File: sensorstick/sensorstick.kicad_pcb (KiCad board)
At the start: 2 copper layers, 85 x 23 mm, 10 parts, among them J1 U217-04XN-XXR84, U1 XIAO-ESP32-C6-SMD, U2 SCD40-D-R2

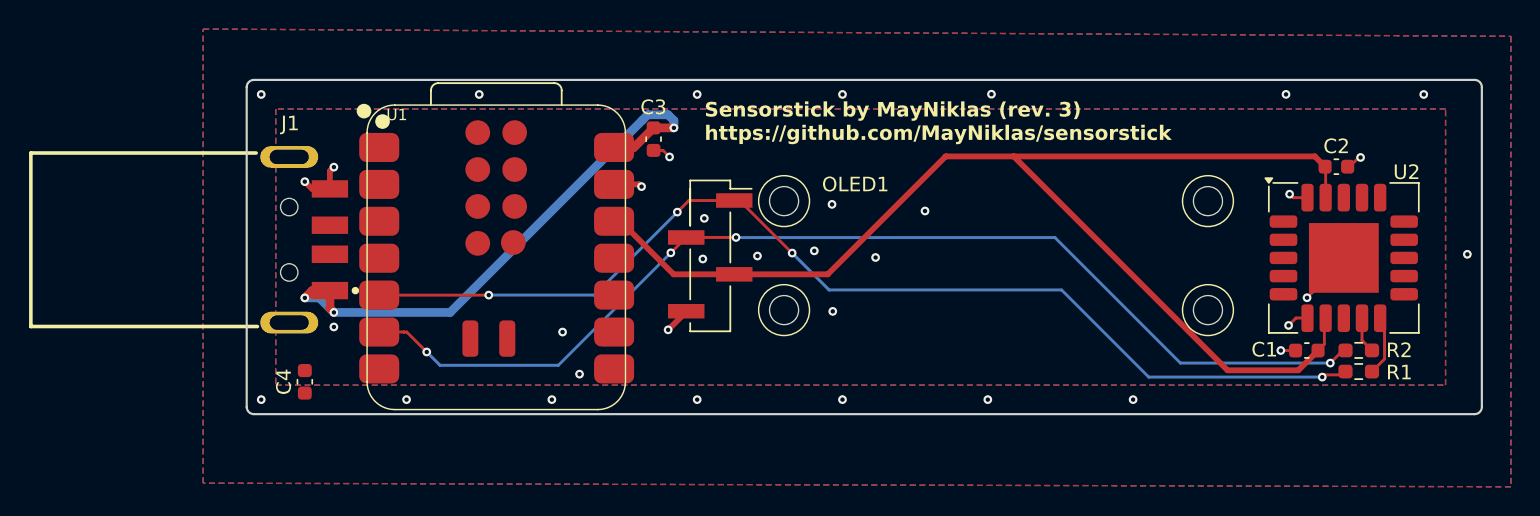
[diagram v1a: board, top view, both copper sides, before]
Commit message: remove unused pads
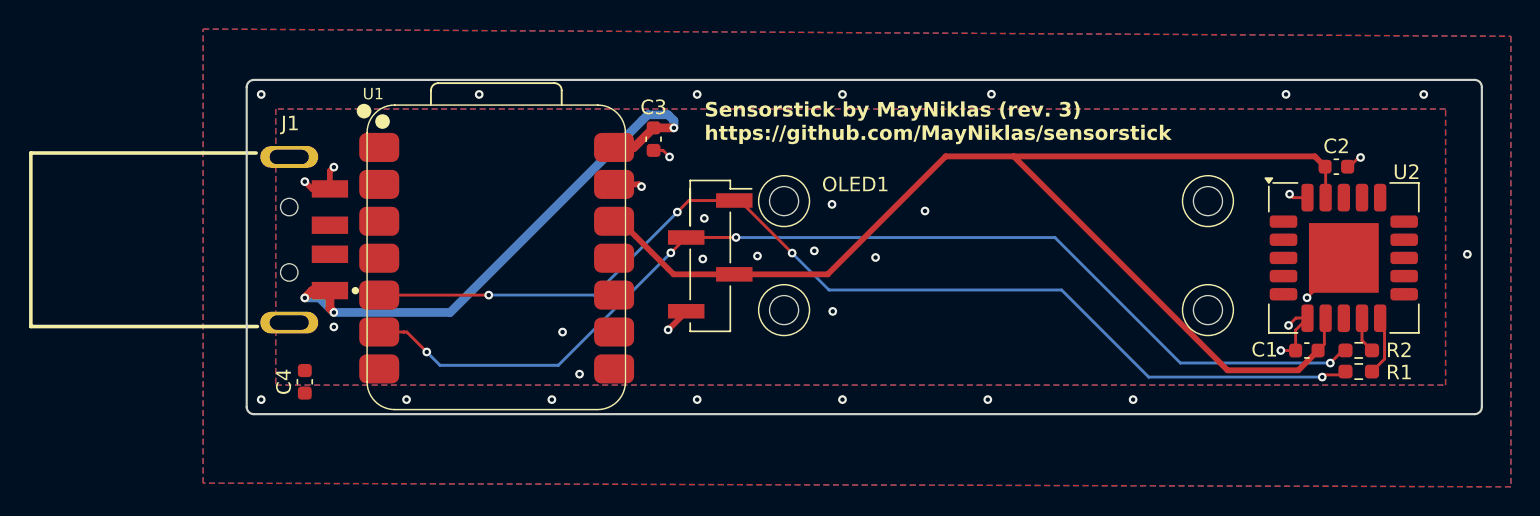
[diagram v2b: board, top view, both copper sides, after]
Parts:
- U1: footprint CustomLibrary:XIAO-ESP32C6-SMD -> CustomLibrary:XIAO-ESP32C6-SMD_no-pad
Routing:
- net GND: track 17.7 -> 20.3 mm
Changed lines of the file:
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@@
 	(net 10 "Net-(U2-SCL)")
 	(net 11 "unconnected-(U1-GPIO18_D10_MOSI-Pad11)")
-	(net 12 "unconnected-(U1-CHIP_EN-Pad19)")
-	(net 13 "unconnected-(U1-GPIO20_D9_MISO-Pad10)")
-	(net 14 "unconnected-(U1-3V3_1-Pad24)")
-	(net 15 "unconnected-(U1-MTDO-Pad18)")
-	(net 16 "unconnected-(U1-MTMS-Pad21)")
-	(net 17 "unconnected-(U1-GPIO19_D8_SCK-Pad9)")
-	(net 18 "unconnected-(U1-GPIO0_A0_D0-Pad1)")
-	(net 19 "unconnected-(U1-GPIO17_D7_RX-Pad8)")
-	(net 20 "unconnected-(U1-GPIO1_A1_D1-Pad2)")
-	(net 21 "unconnected-(U1-GPIO21_D3-Pad4)")
-	(net 22 "unconnected-(U1-GPIO2_A2_D2-Pad3)")
-	(net 23 "unconnected-(U1-MTCK-Pad22)")
-	(net 24 "unconnected-(U1-GPIO16_D6_TX-Pad7)")
-	(net 25 "unconnected-(U1-BOOT-Pad23)")
-	(net 26 "unconnected-(U1-MTDI-Pad17)")
-	(net 27 "unconnected-(U1-GND-Pad20)")
-	(net 28 "unconnected-(U1-GND-Pad16)")
-	(net 29 "unconnected-(U1-BAT-Pad15)")
+	(net 12 "unconnected-(U1-GPIO20_D9_MISO-Pad10)")
+	(net 13 "unconnected-(U1-GPIO19_D8_SCK-Pad9)")
+	(net 14 "unconnected-(U1-GPIO0_A0_D0-Pad1)")
+	(net 15 "unconnected-(U1-GPIO17_D7_RX-Pad8)")
+	(net 16 "unconnected-(U1-GPIO1_A1_D1-Pad2)")
+	(net 17 "unconnected-(U1-GPIO21_D3-Pad4)")
+	(net 18 "unconnected-(U1-GPIO2_A2_D2-Pad3)")
+	(net 19 "unconnected-(U1-GPIO16_D6_TX-Pad7)")
 	(footprint "Capacitor_SMD:C_0603_1608Metric"
 		(layer "F.Cu")
@@
 		)
 	)
-	(footprint "CustomLibrary:XIAO-ESP32C6-SMD"
+	(footprint "CustomLibrary:XIAO-ESP32C6-SMD_no-pad"
 		(layer "F.Cu")
 		(at 77.4 99.7468)
 		(property "Reference" "U1"
-			(at -7.7986 -9.3825 0)
+			(at -9.425 -10.8218 0)
 			(layer "F.SilkS")
 			(effects
@@
 			(layers "F.Cu" "F.Mask" "F.Paste")
 			(roundrect_rratio 0.25)
-			(net 18 "unconnected-(U1-GPIO0_A0_D0-Pad1)")
+			(net 14 "unconnected-(U1-GPIO0_A0_D0-Pad1)")
 			(pinfunction "GPIO0_A0_D0")
 			(pintype "passive+no_connect")
@@
 			(layers "F.Cu" "F.Mask" "F.Paste")
 			(roundrect_rratio 0.25)
-			(net 20 "unconnected-(U1-GPIO1_A1_D1-Pad2)")
+			(net 16 "unconnected-(U1-GPIO1_A1_D1-Pad2)")
 			(pinfunction "GPIO1_A1_D1")
 			(pintype "passive+no_connect")
@@
 			(layers "F.Cu" "F.Mask" "F.Paste")
 			(roundrect_rratio 0.25)
-			(net 22 "unconnected-(U1-GPIO2_A2_D2-Pad3)")
+			(net 18 "unconnected-(U1-GPIO2_A2_D2-Pad3)")
 			(pinfunction "GPIO2_A2_D2")
 			(pintype "passive+no_connect")
@@
 			(layers "F.Cu" "F.Mask" "F.Paste")
 			(roundrect_rratio 0.25)
-			(net 21 "unconnected-(U1-GPIO21_D3-Pad4)")
+			(net 17 "unconnected-(U1-GPIO21_D3-Pad4)")
 			(pinfunction "GPIO21_D3")
 			(pintype "passive+no_connect")
@@
 			(layers "F.Cu" "F.Mask" "F.Paste")
 			(roundrect_rratio 0.25)
-			(net 24 "unconnected-(U1-GPIO16_D6_TX-Pad7)")
+			(net 19 "unconnected-(U1-GPIO16_D6_TX-Pad7)")
 			(pinfunction "GPIO16_D6_TX")
 			(pintype "passive+no_connect")
@@
 			(layers "F.Cu" "F.Mask" "F.Paste")
 			(roundrect_rratio 0.25)
-			(net 19 "unconnected-(U1-GPIO17_D7_RX-Pad8)")
+			(net 15 "unconnected-(U1-GPIO17_D7_RX-Pad8)")
 			(pinfunction "GPIO17_D7_RX")
 			(pintype "passive+no_connect")
@@
 			(layers "F.Cu" "F.Mask" "F.Paste")
 			(roundrect_rratio 0.25)
-			(net 17 "unconnected-(U1-GPIO19_D8_SCK-Pad9)")
+			(net 13 "unconnected-(U1-GPIO19_D8_SCK-Pad9)")
 			(pinfunction "GPIO19_D8_SCK")
 			(pintype "passive+no_connect")
@@
 			(layers "F.Cu" "F.Mask" "F.Paste")
 			(roundrect_rratio 0.25)
-			(net 13 "unconnected-(U1-GPIO20_D9_MISO-Pad10)")
+			(net 12 "unconnected-(U1-GPIO20_D9_MISO-Pad10)")
 			(pinfunction "GPIO20_D9_MISO")
 			(pintype "passive+no_connect")
@@
 			(thermal_bridge_angle 45)
 		)
-		(pad "15" smd roundrect
-			(at -2.008 5.5532 270)
-			(size 2.5 1.1)
-			(layers "F.Cu" "F.Mask" "F.Paste")
-			(roundrect_rratio 0.25)
-			(net 29 "unconnected-(U1-BAT-Pad15)")
-			(pinfunction "BAT")
-			(pintype "passive+no_connect")
-			(solder_mask_margin 0.0508)
-			(thermal_bridge_angle 45)
-		)
-		(pad "16" smd roundrect
-			(at 0.532 5.5532 270)
-			(size 2.5 1.1)
-			(layers "F.Cu" "F.Mask" "F.Paste")
-			(roundrect_rratio 0.25)
-			(net 28 "unconnected-(U1-GND-Pad16)")
-			(pinfunction "GND")
-			(pintype "passive+no_connect")
-			(solder_mask_margin 0.0508)
-			(thermal_bridge_angle 45)
-		)
-		(pad "17" smd circle
-			(at -1.5 -8.62)
-			(size 1.7 1.7)
-			(layers "F.Cu" "F.Mask" "F.Paste")
-			(net 26 "unconnected-(U1-MTDI-Pad17)")
-			(pinfunction "MTDI")
-			(pintype "passive+no_connect")
-		)
-		(pad "18" smd circle
-			(at 1.04 -8.62)
-			(size 1.7 1.7)
-			(layers "F.Cu" "F.Mask" "F.Paste")
-			(net 15 "unconnected-(U1-MTDO-Pad18)")
-			(pinfunction "MTDO")
-			(pintype "passive+no_connect")
-		)
-		(pad "19" smd circle
-			(at -1.5 -6.08)
-			(size 1.7 1.7)
-			(layers "F.Cu" "F.Mask" "F.Paste")
-			(net 12 "unconnected-(U1-CHIP_EN-Pad19)")
-			(pinfunction "CHIP_EN")
-			(pintype "passive+no_connect")
-		)
-		(pad "20" smd circle
-			(at 1.04 -6.08)
-			(size 1.7 1.7)
-			(layers "F.Cu" "F.Mask" "F.Paste")
-			(net 27 "unconnected-(U1-GND-Pad20)")
-			(pinfunction "GND")
-			(pintype "passive+no_connect")
-		)
-		(pad "21" smd circle
-			(at -1.5 -3.54)
-			(size 1.7 1.7)
-			(layers "F.Cu" "F.Mask" "F.Paste")
-			(net 16 "unconnected-(U1-MTMS-Pad21)")
-			(pinfunction "MTMS")
-			(pintype "passive+no_connect")
-		)
-		(pad "22" smd circle
-			(at 1.04 -3.54)
-			(size 1.7 1.7)
-			(layers "F.Cu" "F.Mask" "F.Paste")
-			(net 23 "unconnected-(U1-MTCK-Pad22)")
-			(pinfunction "MTCK")
-			(pintype "passive+no_connect")
-		)
-		(pad "23" smd circle
-			(at -1.5 -1)
-			(size 1.7 1.7)
-			(layers "F.Cu" "F.Mask" "F.Paste")
-			(net 25 "unconnected-(U1-BOOT-Pad23)")
-			(pinfunction "BOOT")
-			(pintype "passive+no_connect")
-		)
-		(pad "24" smd circle
-			(at 0.9474 -1.0568)
-			(size 1.7 1.7)
-			(layers "F.Cu" "F.Mask" "F.Paste")
-			(net 14 "unconnected-(U1-3V3_1-Pad24)")
-			(pinfunction "3V3_1")
-			(pintype "passive+no_connect")
-		)
 		(embedded_fonts no)
 		(model "${KIPRJMOD}/CustomLibrary.pretty/3d-models/Seeed Studio XIAO ESP32-C6.step"
@@
 	)
 	(segment
+		(start 132.181 104.719)
+		(end 133 103.9)
+		(width 0.2)
+		(layer "F.Cu")
+		(net 1)
+	)
+	(segment
 		(start 135.5 99.958)
 		(end 135.5 99.75)
@@
 		(width 0.2)
 		(layer "F.Cu")
+		(net 1)
+	)
+	(segment
+		(start 132.181 106.1212)
+		(end 132.181 104.719)
+		(width 0.2)
+		(layer "F.Cu")

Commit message: use footprint without pads
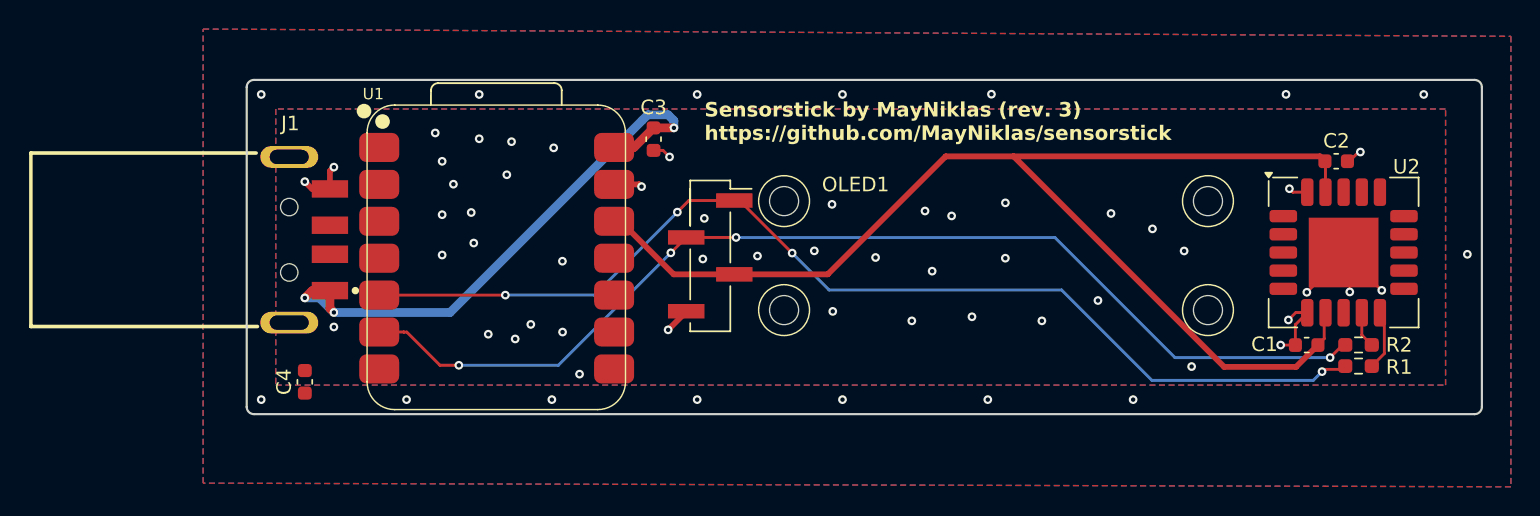
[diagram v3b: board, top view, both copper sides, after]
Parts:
- moved C2 0.38 mm to (135.0, 93.1)
- moved R1 0.38 mm to (136.5, 107.2)
- moved R2 0.38 mm to (136.5, 105.7)
- moved U2 0.38 mm to (135.5, 99.4)
- moved C1 0.38 mm to (132.9, 105.7)
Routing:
- net GND: track 20.3 -> 26.9 mm, vias 21 -> 50
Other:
- board text added: "{ "ViaStitching": "0.2", "GND": { "HSpacing": "3", "VSpacing": "3", "HOffset": "0", "VOffset": "0", "Clearance": "2", "Randomize": false } }"

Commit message: fix I2C resistors
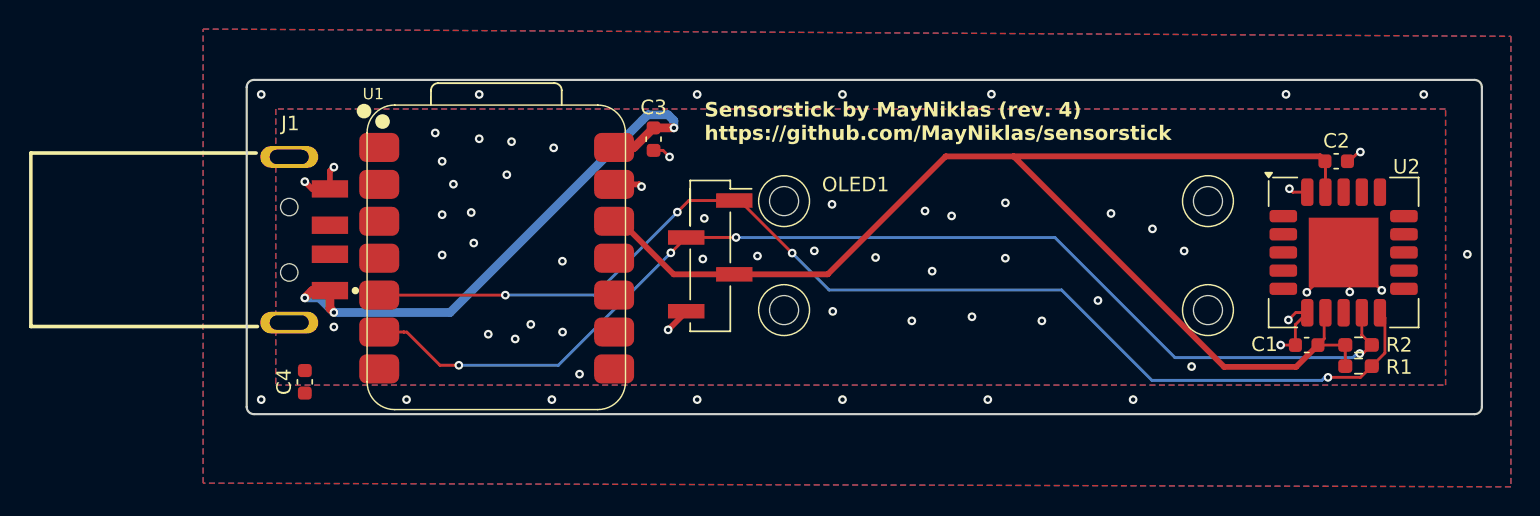
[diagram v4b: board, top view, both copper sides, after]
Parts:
- U1: value XIAO-ESP32-C6-SMD -> XIAO-ESP32-C6
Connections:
- R1 pad 1: Net-(U2-SDA) -> /IC2_SDA
- R1 pad 2: /IC2_SDA -> +3.3V
- R2 pad 1: Net-(U2-SCL) -> /I2C_SCL
- R2 pad 2: /I2C_SCL -> +3.3V
- U2 pad 10: Net-(U2-SDA) -> /IC2_SDA
- U2 pad 9: Net-(U2-SCL) -> /I2C_SCL
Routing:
- net /IC2_SDA: track 75.0 -> 81.0 mm
- net /I2C_SCL: track 75.0 -> 79.2 mm
- net Net-(U2-SDA): track 4.15 -> 0.00 mm
- net +3.3V: track 86.1 -> 89.9 mm
- net Net-(U2-SCL): track 2.50 -> 0.00 mm
